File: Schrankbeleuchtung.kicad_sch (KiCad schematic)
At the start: 27 parts, among them J1 Jack-DC, J2 Conn_01x02, J3 Conn_01x02, J4 Conn_01x02, J5 Conn_01x02, J6 Conn_01x02, J7 Conn_01x02, J8 Conn_01x02, J9 Conn_01x02, Q1 AO3400A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

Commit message: Edit description
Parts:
- J2: Name (none) -> LED 1
- J3: Name (none) -> LED 2
- J4: Name (none) -> LED 3
- J5: Name (none) -> LED 4
- J6: Name (none) -> Sensor 1
- J7: Name (none) -> Sensor 2
- J8: Name (none) -> Sensor 3
- J9: Name (none) -> Sensor 4
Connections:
- no-connect marks 2 -> 24
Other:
- title: (none) -> Schrankbeleuchtung
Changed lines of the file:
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@@
 	(generator_version "9.0")
 	(paper "A4")
+	(title_block
+		(title "Schrankbeleuchtung")
+		(date "2025-06-08")
+	)
 	(junction
 		(at 254 115.57)
@@
 	)
 	(no_connect
+		(at 59.69 125.73)
+	)
+	(no_connect
+		(at 59.69 133.35)
+	)
+	(no_connect
+		(at 105.41 140.97)
+	)
+	(no_connect
+		(at 59.69 161.29)
+	)
+	(no_connect
+		(at 105.41 138.43)
+	)
+	(no_connect
+		(at 105.41 143.51)
+	)
+	(no_connect
+		(at 59.69 168.91)
+	)
+	(no_connect
+		(at 105.41 153.67)
+	)
+	(no_connect
+		(at 105.41 148.59)
+	)
+	(no_connect
+		(at 105.41 168.91)
+	)
+	(no_connect
+		(at 105.41 133.35)
+	)
+	(no_connect
 		(at 50.8 63.5)
 	)
 	(no_connect
+		(at 105.41 163.83)
+	)
+	(no_connect
+		(at 105.41 146.05)
+	)
+	(no_connect
+		(at 59.69 123.19)
+	)
+	(no_connect
+		(at 59.69 163.83)
+	)
+	(no_connect
+		(at 59.69 158.75)
+	)
+	(no_connect
+		(at 105.41 161.29)
+	)
+	(no_connect
+		(at 59.69 166.37)
+	)
+	(no_connect
+		(at 105.41 135.89)
+	)
+	(no_connect
+		(at 59.69 156.21)
+	)
+	(no_connect
+		(at 59.69 130.81)
+	)
+	(no_connect
 		(at 76.2 63.5)
 	)
+	(no_connect
+		(at 105.41 158.75)
+	)
 	(wire
 		(pts
@@
 		(on_board yes)
 		(dnp no)
-		(fields_autoplaced yes)
 		(property "Reference" "J9"
 			(at 267.97 149.8599 0)
@@
 			)
 		)
+		(property "Name" "Sensor 4"
+			(at 265.43 147.32 0)
+			(effects
+				(font
+					(size 1.27 1.27)
+				)
+			)
+		)
 		(pin "2"
 		)
@@
 		(on_board yes)
 		(dnp no)
-		(fields_autoplaced yes)
 		(property "Reference" "J8"
 			(at 204.47 149.8599 0)
@@
 			)
 		)
+		(property "Name" "Sensor 3"
+			(at 201.93 147.32 0)
+			(effects
+				(font
+					(size 1.27 1.27)
+				)
+			)
+		)
 		(pin "2"
 		)
@@
 		(on_board yes)
 		(dnp no)
-		(fields_autoplaced yes)
 		(property "Reference" "J4"
 			(at 204.47 59.6899 0)
@@
 			)
 		)
+		(property "Name" "LED 3"
+			(at 201.93 57.15 0)
+			(effects
+				(font
+					(size 1.27 1.27)
+				)
+			)
+		)
 		(pin "2"
 		)
@@
 		(on_board yes)
 		(dnp no)
-		(fields_autoplaced yes)
 		(property "Reference" "J6"
 			(at 204.47 115.5699 0)
@@
 			)
 		)
+		(property "Name" "Sensor 1"
+			(at 201.93 113.03 0)
+			(effects
+				(font
+					(size 1.27 1.27)
+				)
+			)
+		)
 		(pin "2"
 		)
@@
 		(on_board yes)
 		(dnp no)
-		(fields_autoplaced yes)
 		(property "Reference" "J2"
 			(at 204.47 24.1299 0)
@@
 			)
 		)
+		(property "Name" "LED 1"
+			(at 201.93 20.574 0)
+			(effects
+				(font
+					(size 1.27 1.27)
+				)
+				(justify top)
+			)
+		)
 		(pin "2"
 		)
@@
 		(on_board yes)
 		(dnp no)
-		(fields_autoplaced yes)
 		(property "Reference" "J7"
 			(at 267.97 115.5699 0)
@@
 			)
 		)
+		(property "Name" "Sensor 2"
+			(at 265.43 113.03 0)
+			(effects
+				(font
+					(size 1.27 1.27)
+				)
+			)
+		)
 		(pin "2"
 		)
@@
 		(on_board yes)
 		(dnp no)
-		(fields_autoplaced yes)
 		(property "Reference" "J3"
 			(at 269.24 24.1299 0)
@@
 			)
 		)
+		(property "Name" "LED 2"
+			(at 266.7 21.59 0)
+			(effects
+				(font
+					(size 1.27 1.27)
+				)
+			)
+		)
 		(pin "2"
 		)
@@
 		(on_board yes)
 		(dnp no)
-		(fields_autoplaced yes)
 		(property "Reference" "J5"
 			(at 269.24 59.6899 0)
@@
 			)
 		)
+		(property "Name" "LED 4"
+			(at 266.7 57.15 0)
+			(effects
+				(font
+					(size 1.27 1.27)
+				)
+			)
+		)

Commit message: Edit PCB layout
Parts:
- removed C1: 220µF, Capacitor_SMD:C_1206_3216Metric, symbol Device:C
- removed J1: Jack-DC, Connector_BarrelJack:BarrelJack_GCT_DCJ200-10-A_Horizontal, symbol Connector:Jack-DC
- removed Q1, Q2, Q3, Q4: AO3400A, Package_TO_SOT_SMD:SOT-23, symbol Transistor_FET:AO3400A
- added C1: 100µF, Capacitor_SMD:CP_Elec_6.3x5.8, symbol Device:C_Polarized
- added H1, H2, H3: MountingHole_Pad, MountingHole:MountingHole_2.2mm_M2_ISO7380_Pad, symbol Mechanical:MountingHole_Pad
- added J1: 694106301002, Connector_BarrelJack:BarrelJack_Horizontal, symbol Connector:Barrel_Jack_Switch
- added Q1, Q2, Q3, Q4: IRLML6344, Package_TO_SOT_SMD:SOT-23, symbol Transistor_FET:BSS123
- A1: value RaspberryPi_Pico -> SC0918
- C2: value 220µF -> 100µF; footprint Capacitor_SMD:C_1206_3216Metric -> Capacitor_SMD:C_1210_3225Metric
- J2, J3, J4, J5, J6, J7, J8, J9: value Conn_01x02 -> B2B-XH-AMLFSNP
- L1: value DR127-330-R -> 33µH; footprint footprints:IND_DR127-330-R_EAT -> Inductor_SMD:L_7.3x7.3_H3.5
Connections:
- net +12V: now also C1.1, J1.1
- net GND: now also C1.2, H1.1, H2.1, H3.1, J1.2, Q1.2 (S), Q2.2 (S), Q3.2 (S), Q4.2 (S)
- net at J4.2 (Pin_2): now also Q3.3 (D)
- net at R4.2: now also Q4.1 (G)
- net at R3.2: now also Q3.1 (G)
- net at J2.2 (Pin_2): now also Q1.3 (D)
- net at J3.2 (Pin_2): now also Q2.3 (D)
- net at J5.2 (Pin_2): now also Q4.3 (D)
- net at R2.2: now also Q2.1 (G)
- net at R1.2: now also Q1.1 (G)
- no-connect marks 24 -> 25
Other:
- moved on the sheet: J2, J3, J4, J5, J6, J7, J8, J9, R1, R2, R3, R4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

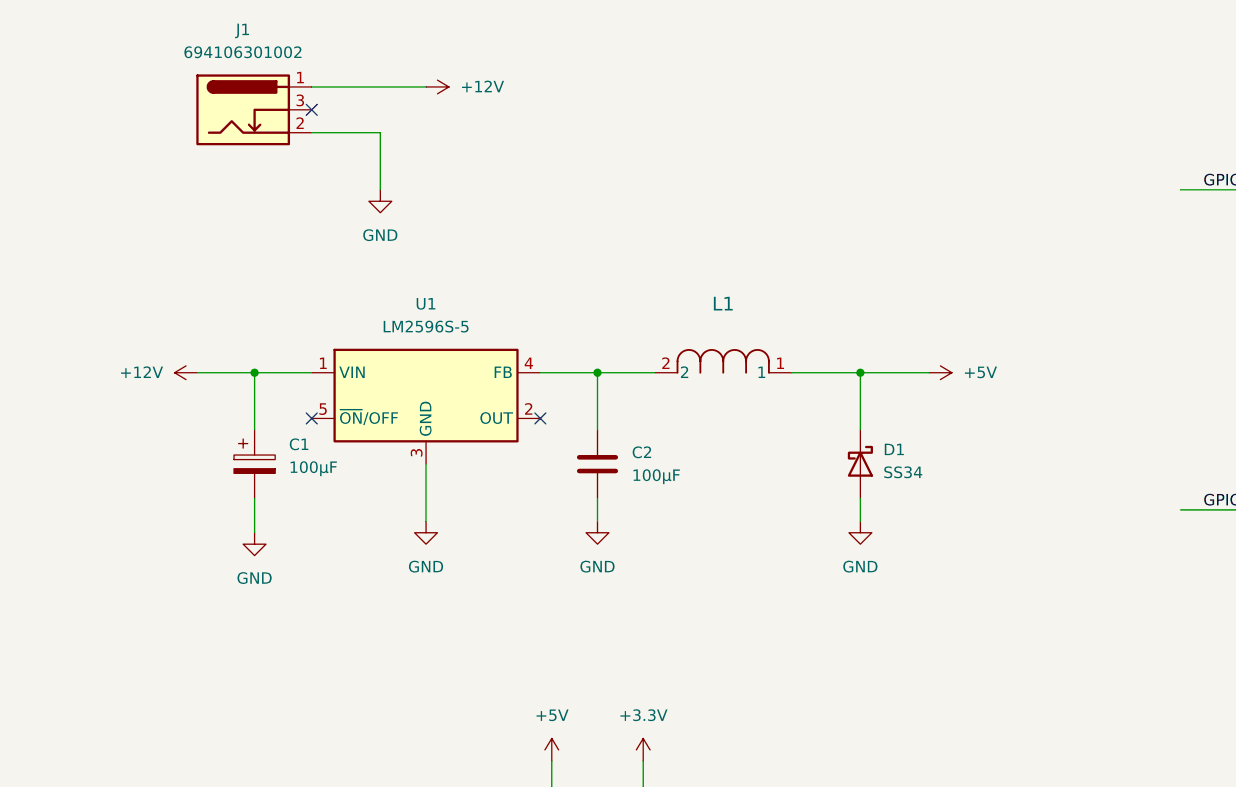
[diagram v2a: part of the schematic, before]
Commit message: Spannungswandler geändert. Stückliste aktualisiert.
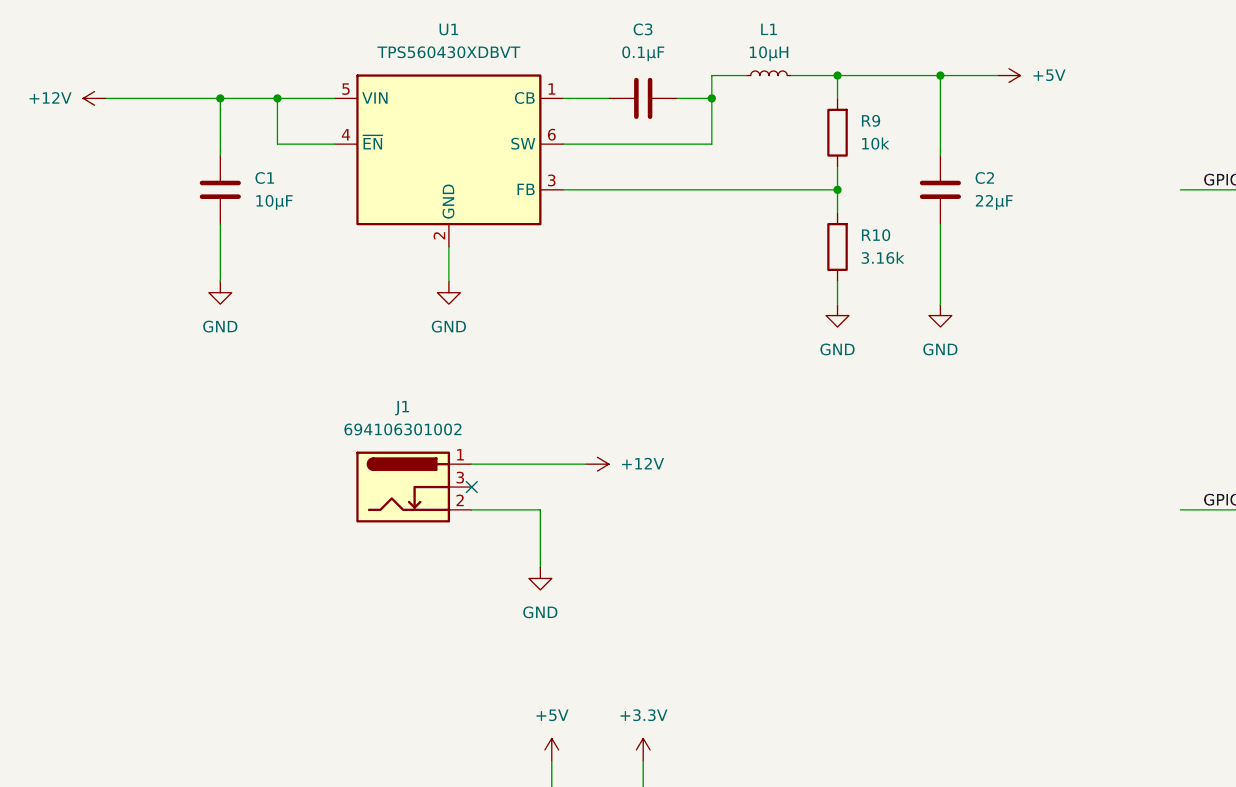
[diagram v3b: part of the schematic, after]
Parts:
- removed C1: 100µF, Capacitor_SMD:CP_Elec_6.3x5.8, symbol Device:C_Polarized
- removed D1: SS34, Diode_SMD:D_SMA, symbol Diode:SS34
- removed L1: 33µH, Inductor_SMD:L_7.3x7.3_H3.5, symbol IND_DR127-330-R_EAT:DR127-330-R
- added C1: 10µF, Capacitor_SMD:C_0805_2012Metric_Pad1.18x1.45mm_HandSolder, symbol Device:C
- added C3: 0.1µF, Capacitor_SMD:C_0805_2012Metric_Pad1.18x1.45mm_HandSolder, symbol Device:C
- added L1: 10µH, Inductor_SMD:L_Cenker_CKCS4030, symbol Device:L_Small
- added R10: 3.16k, Resistor_SMD:R_0805_2012Metric_Pad1.20x1.40mm_HandSolder, symbol Device:R
- added R9: 10k, Resistor_SMD:R_0805_2012Metric_Pad1.20x1.40mm_HandSolder, symbol Device:R
- C2: value 100µF -> 22µF; footprint Capacitor_SMD:C_1210_3225Metric -> Capacitor_SMD:C_0805_2012Metric_Pad1.18x1.45mm_HandSolder; Mouser (none) -> 81-GRM21BZ71A226ME5L
- R1, R2, R3, R4, R5, R6, R7, R8: footprint Resistor_SMD:R_0805_2012Metric -> Resistor_SMD:R_0805_2012Metric_Pad1.20x1.40mm_HandSolder
- U1: value LM2596S-5 -> TPS560430XDBVT; footprint Package_TO_SOT_SMD:TO-263-5_TabPin3 -> Package_TO_SOT_SMD:SOT-23-6_Handsoldering; Mouser (none) -> 595-TPS560430XDBVT
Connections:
- net +12V: now also U1.4 (~{EN}), U1.5 (VIN), C1.1; no longer U1.1 (VIN)
- net +5V: now also C2.1, L1.2, R9.2
- net GND: now also U1.2 (GND), C1.2, R10.1; no longer U1.3 (GND)
- new net: R10.2, R9.1, U1.3 (FB)
- new net: C3.1, U1.1 (CB)
- new net: C3.2, L1.1, U1.6 (SW)
- no-connect marks 25 -> 23
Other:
- moved on the sheet: C2, J1

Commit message: PCB Layoutupdate
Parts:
- added H4: MountingHole_Pad, MountingHole:MountingHole_2.2mm_M2_ISO7380_Pad, symbol Mechanical:MountingHole_Pad
- J2, J3, J4, J5, J6, J7, J8, J9: footprint Connector_JST:JST_XH_B2B-XH-AM_1x02_P2.50mm_Vertical -> Connector_JST:JST_XH_B2B-XH-A_1x02_P2.50mm_Vertical
- Q1, Q2, Q3, Q4: value IRLML6344 -> IRLML0030TRPBF
- R1, R2, R3, R4: value 100R -> 187R
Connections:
- net GND: now also H4.1
- net GPIO06: now also A1.12 (GPIO9); no longer A1.9 (GPIO6)
- net GPIO07: now also A1.14 (GPIO10); no longer A1.10 (GPIO7)
- net GPIO08: now also A1.15 (GPIO11); no longer A1.11 (GPIO8)
- net GPIO09: now also A1.16 (GPIO12); no longer A1.12 (GPIO9)
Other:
- moved on the sheet: H1, H2, H3
